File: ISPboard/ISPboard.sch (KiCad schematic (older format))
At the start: 17 parts, among them IC1 ATMEGA328-P, P1 5V, P2 ISP, P3 PB, P4 PC, P5 PD, P6 LED OUT, P7 BUTTON OUT, SW1 PUSH 1, SW2 PUSH 2

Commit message: Added the avr alarm project
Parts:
- added C1: 0.33uF, Capacitors_ThroughHole:C_Radial_D10_L20_P5, symbol C
- added C2: 0.1uF, Capacitors_ThroughHole:C_Radial_D10_L20_P7.5, symbol C
- added R4, R5: 10k, Resistors_ThroughHole:Resistor_Vertical_RM5mm, symbol R
- added U1: LM7805CT, TO_SOT_Packages_THT:TO-220_Neutral123_Horizontal, symbol LM7805CT
- P1: value 5V -> CONN_01X02
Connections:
- net GND: now also C1.2, C2.2, U1.2 (GND)
- net VCC: now also D1.2 (A), P1.2 (P2); no longer D1.1 (K), IC1.20 (AVCC), IC1.7 (VCC), P2.2 (P2), R3.2
- net at P7.1 (P1), SW2.1: now also R5.1
- net at P7.2 (P2), SW1.1: now also R4.2
- new net: C1.1, D1.1 (K), U1.1 (IN)
- new net VDD: C2.1, IC1.20 (AVCC), IC1.7 (VCC), P2.2 (P2), R3.2, R4.1, R5.2, U1.3 (OUT)
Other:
- note added: "ISP connector"
- note added: "Microcontroller"
- note added: "Peripherals"
- note added: "Power"
- moved on the sheet: D2, D3, D4, IC1, P2, P3, P4, P5, P6, P7, R1, R2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

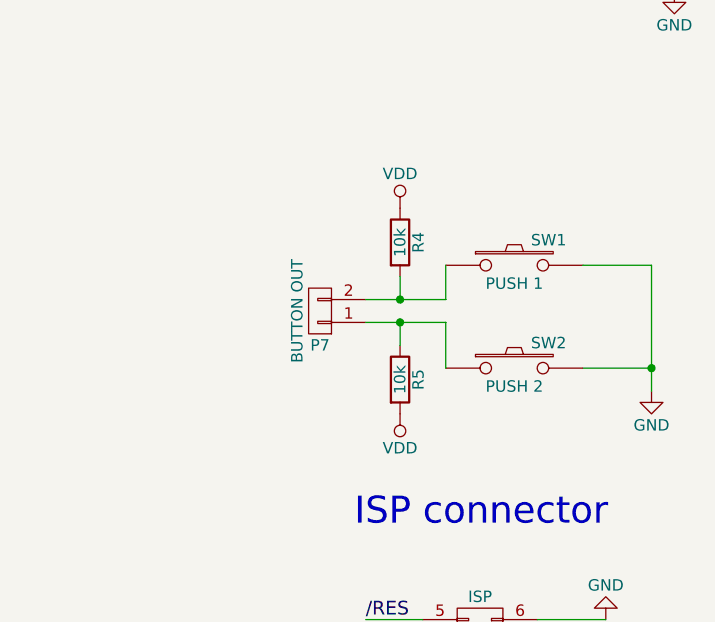
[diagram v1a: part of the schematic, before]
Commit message: Got display working on AVRAlarm
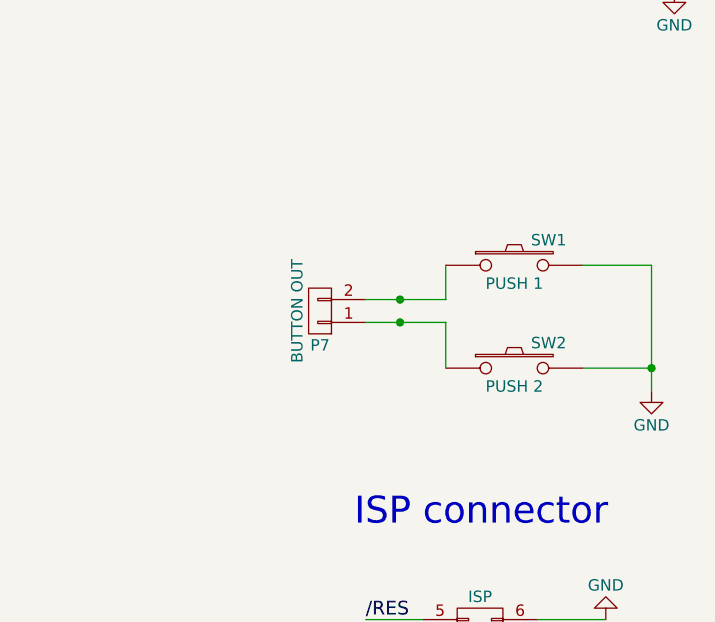
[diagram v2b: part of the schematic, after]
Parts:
- removed R4, R5: 10k, Resistors_ThroughHole:Resistor_Vertical_RM5mm, symbol R
- C1: footprint Capacitors_ThroughHole:C_Radial_D10_L20_P5 -> Capacitors_SMD:C_1206_HandSoldering
- C2: footprint Capacitors_ThroughHole:C_Radial_D10_L20_P7.5 -> Capacitors_SMD:C_1206_HandSoldering
- R1, R2, R3: footprint Resistors_ThroughHole:Resistor_Vertical_RM5mm -> Resistors_SMD:R_1206_HandSoldering
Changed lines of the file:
@@
 F 0 "R1" V 9680 1700 50  0000 C CNN
 F 1 "R" V 9600 1700 50  0000 C CNN
-F 2 "Resistors_ThroughHole:Resistor_Vertical_RM5mm" V 9530 1700 50  0001 C CNN
+F 2 "Resistors_SMD:R_1206_HandSoldering" V 9530 1700 50  0001 C CNN
 F 3 "" H 9600 1700 50  0000 C CNN
 	1    9600 1700
@@
 F 0 "R2" V 9680 1800 50  0000 C CNN
 F 1 "R" V 9600 1800 50  0000 C CNN
-F 2 "Resistors_ThroughHole:Resistor_Vertical_RM5mm" V 9530 1800 50  0001 C CNN
+F 2 "Resistors_SMD:R_1206_HandSoldering" V 9530 1800 50  0001 C CNN
 F 3 "" H 9600 1800 50  0000 C CNN
 	1    9600 1800
@@
 F 0 "R3" V 980 2850 50  0000 C CNN
 F 1 "R" V 900 2850 50  0000 C CNN
-F 2 "Resistors_ThroughHole:Resistor_Vertical_RM5mm" V 830 2850 50  0001 C CNN
+F 2 "Resistors_SMD:R_1206_HandSoldering" V 830 2850 50  0001 C CNN
 F 3 "" H 900 2850 50  0000 C CNN
 	1    900  2850
@@
 F 0 "C1" H 3125 2250 50  0000 L CNN
 F 1 "0.33uF" H 3125 2050 50  0000 L CNN
-F 2 "Capacitors_ThroughHole:C_Radial_D10_L20_P5" H 3138 2000 50  0001 C CNN
+F 2 "Capacitors_SMD:C_1206_HandSoldering" H 3138 2000 50  0001 C CNN
 F 3 "" H 3100 2150 50  0000 C CNN
 	1    3100 2150
@@
 F 0 "C2" H 4375 2250 50  0000 L CNN
 F 1 "0.1uF" H 4375 2050 50  0000 L CNN
-F 2 "Capacitors_ThroughHole:C_Radial_D10_L20_P7.5" H 4388 2000 50  0001 C CNN
+F 2 "Capacitors_SMD:C_1206_HandSoldering" H 4388 2000 50  0001 C CNN
 F 3 "" H 4350 2150 50  0000 C CNN
 	1    4350 2150
@@
 $EndComp
 $Comp
-L VDD #PWR015
+L VDD #PWR014
 U 1 1 5849F276
 P 750 2850
-F 0 "#PWR015" H 750 2700 50  0001 C CNN
+F 0 "#PWR014" H 750 2700 50  0001 C CNN
 F 1 "VDD" H 750 3000 50  0000 C CNN
 F 2 "" H 750 2850 50  0000 C CNN
@@
 $EndComp
 $Comp
-L VDD #PWR016
+L VDD #PWR015
 U 1 1 5849F2D2
 P 950 4650
-F 0 "#PWR016" H 950 4500 50  0001 C CNN
+F 0 "#PWR015" H 950 4500 50  0001 C CNN
 F 1 "VDD" H 950 4800 50  0000 C CNN
 F 2 "" H 950 4650 50  0000 C CNN
@@
 	-1   0    0    -1
 $EndComp
-$Comp
-L R R4
-U 1 1 5849F77B
-P 9200 3000
-F 0 "R4" V 9280 3000 50  0000 C CNN
-F 1 "10k" V 9200 3000 50  0000 C CNN
-F 2 "Resistors_ThroughHole:Resistor_Vertical_RM5mm" V 9130 3000 50  0001 C CNN
-F 3 "" H 9200 3000 50  0000 C CNN
-	1    9200 3000
-	1    0    0    -1
-$EndComp
-$Comp
-L R R5
-U 1 1 5849F7CD
-P 9200 3600
-F 0 "R5" V 9280 3600 50  0000 C CNN
-F 1 "10k" V 9200 3600 50  0000 C CNN
-F 2 "Resistors_ThroughHole:Resistor_Vertical_RM5mm" V 9130 3600 50  0001 C CNN
-F 3 "" H 9200 3600 50  0000 C CNN
-	1    9200 3600
-	1    0    0    -1
-$EndComp
-Wire Wire Line
-	9200 3350 9200 3450
 Connection ~ 9200 3350
-Wire Wire Line
-	9200 3150 9200 3250
 Connection ~ 9200 3250
 $Comp
-L VDD #PWR017
-U 1 1 5849F8B7
-P 9200 2850
-F 0 "#PWR017" H 9200 2700 50  0001 C CNN
-F 1 "VDD" H 9200 3000 50  0000 C CNN
-F 2 "" H 9200 2850 50  0000 C CNN
-F 3 "" H 9200 2850 50  0000 C CNN
-	1    9200 2850
-	1    0    0    -1
-$EndComp
-$Comp
 L VDD #PWR018
-U 1 1 5849F90B
-P 9200 3750
-F 0 "#PWR018" H 9200 3600 50  0001 C CNN
-F 1 "VDD" H 9200 3900 50  0000 C CNN
-F 2 "" H 9200 3750 50  0000 C CNN
-F 3 "" H 9200 3750 50  0000 C CNN
-	1    9200 3750
-	-1   0    0    1
-$EndComp
-$Comp
-L VDD #PWR019
 U 1 1 584A0970
 P 10100 4850
-F 0 "#PWR019" H 10100 4700 50  0001 C CNN
+F 0 "#PWR018" H 10100 4700 50  0001 C CNN
 F 1 "VDD" H 10100 5000 50  0000 C CNN
 F 2 "" H 10100 4850 50  0000 C CNN
@@
 	2600 2800 2600 2900
 $Comp
-L VCC #PWR?
+L VCC #PWR019
 U 1 1 584A0F4B
 P 2500 2900
-F 0 "#PWR?" H 2500 2750 50  0001 C CNN
+F 0 "#PWR019" H 2500 2750 50  0001 C CNN
 F 1 "VCC" H 2500 3050 50  0000 C CNN
 F 2 "" H 2500 2900 50  0000 C CNN

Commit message: Fine tuned ispboard v2.
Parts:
- removed D1: D_Schottky, Diodes_ThroughHole:Diode_DO-41_SOD81_Vertical_KathodeUp, symbol D_Schottky
- removed U1: LM7805CT, TO_SOT_Packages_THT:TO-220_Neutral123_Horizontal, symbol LM7805CT
- added C3: 22uF, Capacitors_SMD:c_elec_4x4.5, symbol C
- added CBOOT1: 10nF, Capacitors_SMD:C_0805_HandSoldering, symbol C
- added CIN1: 10uF, Capacitors_SMD:c_elec_4x4.5, symbol C
- added Css1: 0.1uF, Capacitors_SMD:C_0805_HandSoldering, symbol C
- added L1: 15uH, Choke_SMD:Choke_SMD_Wuerth-WE-PD2-Typ-L, symbol INDUCTOR_SMALL
- added P8: CONN_01X02, Connectors_Molex:Molex_KK-6410-02_02x2.54mm_Straight, symbol CONN_01X02
- added R4: 45.3k, Resistors_SMD:R_1206_HandSoldering, symbol R
- added R5: 100k, Resistors_SMD:R_1206_HandSoldering, symbol R
- added R6: 10k, Resistors_SMD:R_1206_HandSoldering, symbol R
- added REG1: RT8284, Power_Integrations:SO-8, symbol RT8284
- added Rc1: 13k, Resistors_SMD:R_1206_HandSoldering, symbol R
- C1: value 0.33uF -> 3.3nF; footprint Capacitors_SMD:C_1206_HandSoldering -> Capacitors_SMD:C_0805_HandSoldering
- C2: value 0.1uF -> 22uF; footprint Capacitors_SMD:C_1206_HandSoldering -> Capacitors_SMD:c_elec_4x4.5
- P1: footprint Connectors_Molex:Molex_KK-6410-02_02x2.54mm_Straight -> Socket_Strips:Socket_Strip_Straight_1x02
- P2: footprint Pin_Headers:Pin_Header_Straight_2x03 -> Socket_Strips:Socket_Strip_Straight_2x03
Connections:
- net GND: now also C3.2, CIN1.2, Css1.1, R6.1, REG1.4 (GND), Rc1.2; no longer C1.2
- net VCC: now also CIN1.1, R5.1, REG1.2 (VIN)
- net VDD: now also C3.1, L1.2, R4.1
- net RX: now reaches IC1.2 ((PCINT16/RXD)PD0)
- net RX: now also P8.2 (P2)
- net TX: now reaches IC1.3 ((PCINT17/TXD)PD1)
- net TX: now also P8.1 (P1)
- net at C1.1: now also Rc1.1
- net PB0 renamed PB6
- net PB1 renamed PB7
- net PD0 renamed PD3
- net PD1 renamed PD2
- new net: CBOOT1.1, REG1.1 (BOOT)
- new net: CBOOT1.2, L1.1, REG1.3 (SW)
- new net: R4.2, R6.2, REG1.5 (FB)
- new net: C1.2, REG1.6 (COMP)
- new net: R5.2, REG1.7 (EN)
- new net: Css1.2, REG1.8 (SS)
- no-connect marks 15 -> 13
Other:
- note added: "Battery connector"
- note added: "PWR LED"
- note added: "USART connector"
- note added: "VDD=5V"
- moved on the sheet: D4, P1, R3
